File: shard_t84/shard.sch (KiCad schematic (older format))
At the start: 7 parts, among them J0 Shard, J1 ISP, U1 ATtiny84-20PU

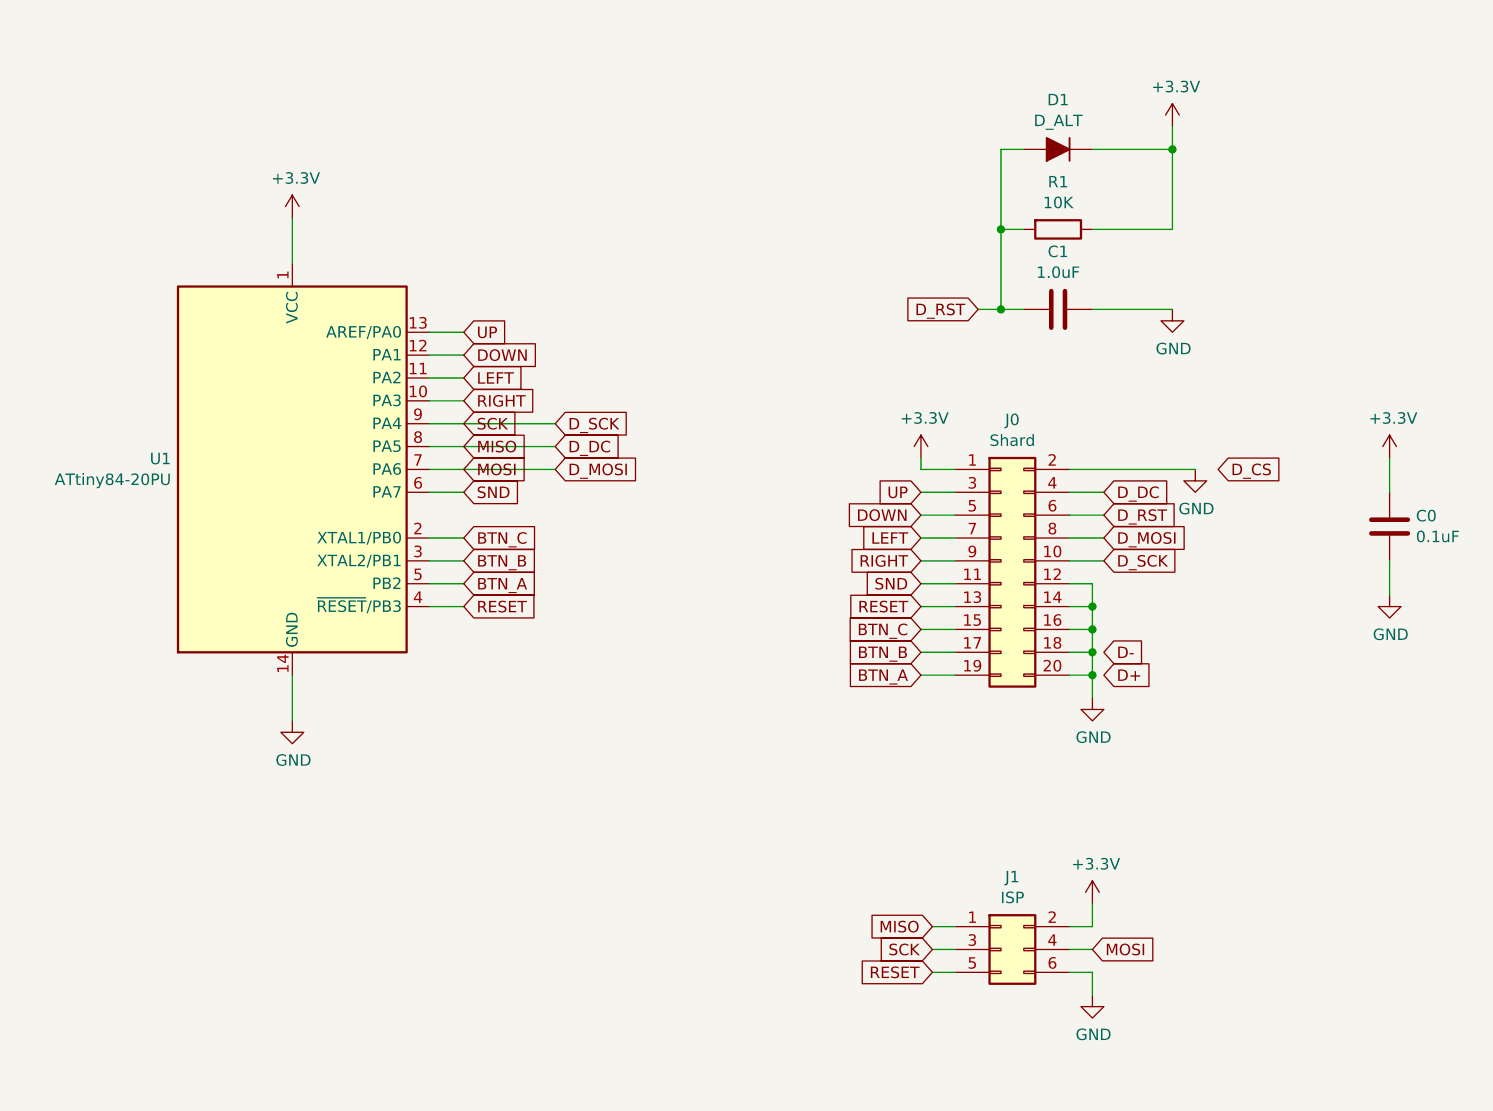
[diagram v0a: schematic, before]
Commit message: t84 shard updated for new layout
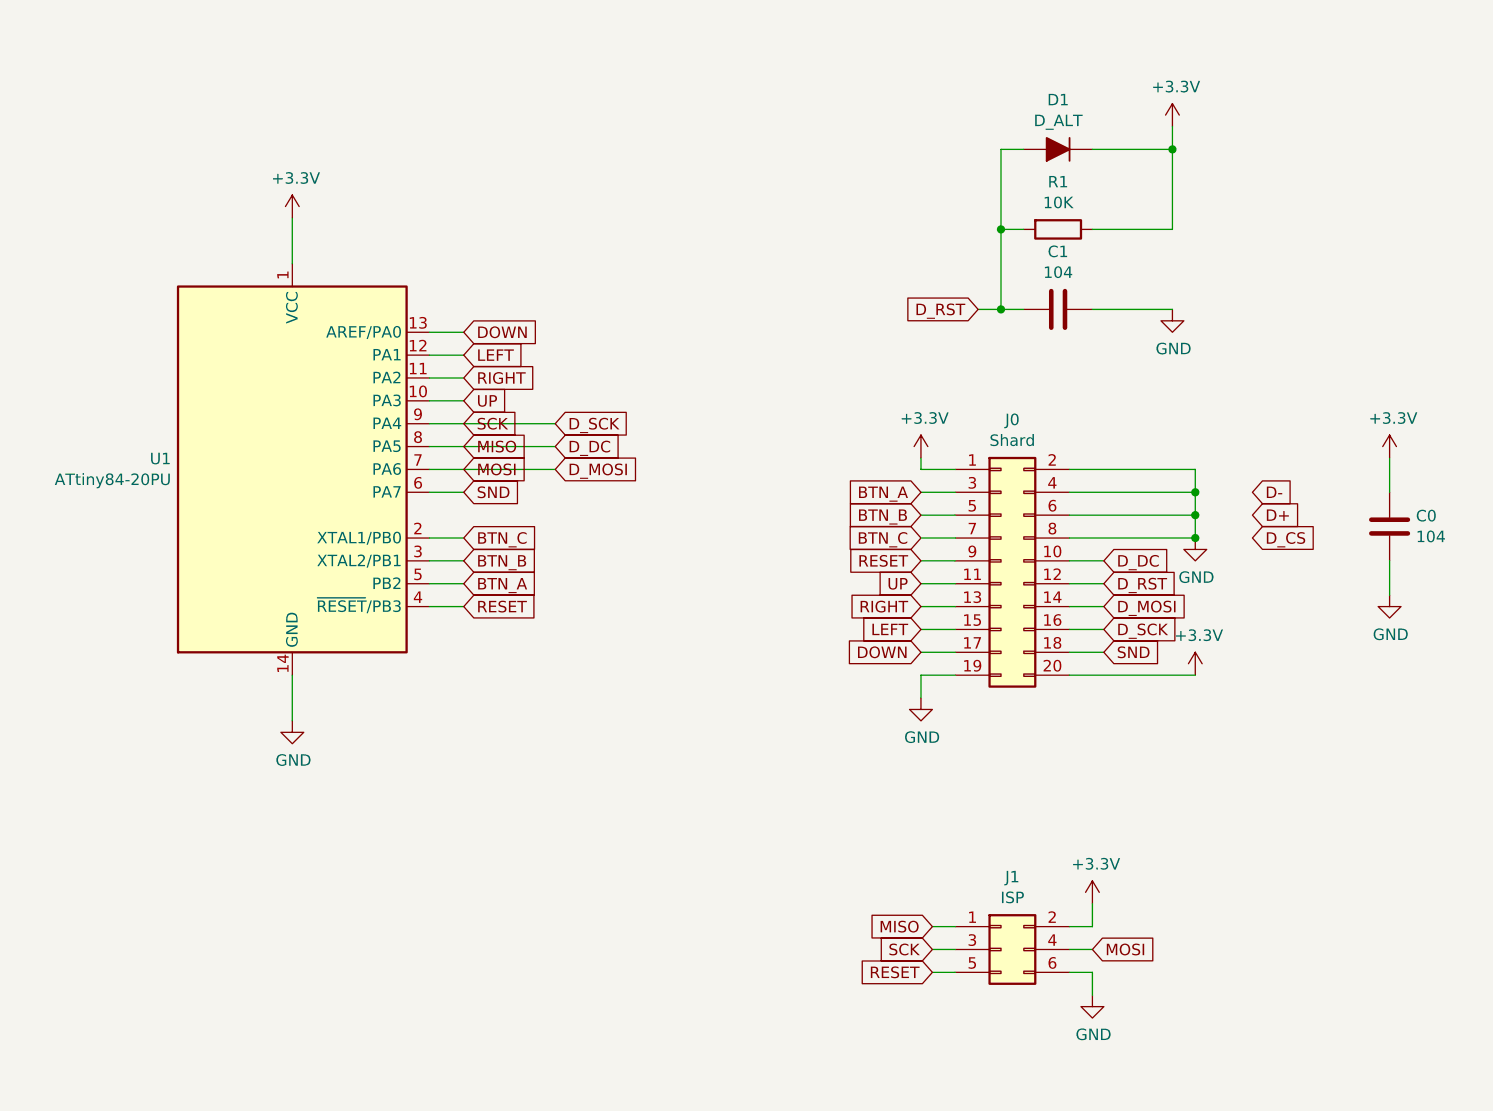
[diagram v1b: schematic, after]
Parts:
- C0: value 0.1uF -> 104
- C1: value 1.0uF -> 104
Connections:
- net +3V3: now also J0.20 (Pin_20)
- net BTN_A: now also J0.3 (Pin_3); no longer J0.19 (Pin_19)
- net BTN_B: now also J0.5 (Pin_5); no longer J0.17 (Pin_17)
- net BTN_C: now also J0.7 (Pin_7); no longer J0.15 (Pin_15)
- net DOWN: now also J0.17 (Pin_17), U1.13 (AREF/PA0); no longer J0.5 (Pin_5), U1.12 (PA1)
- net D_DC: now also J0.10 (Pin_10); no longer J0.4 (Pin_4)
- net D_MOSI: now also J0.14 (Pin_14); no longer J0.8 (Pin_8)
- net D_RST: now also J0.12 (Pin_12); no longer J0.6 (Pin_6)
- net D_SCK: now also J0.16 (Pin_16); no longer J0.10 (Pin_10)
- net GND: now also J0.19 (Pin_19), J0.4 (Pin_4), J0.6 (Pin_6), J0.8 (Pin_8); no longer J0.12 (Pin_12), J0.14 (Pin_14), J0.16 (Pin_16), J0.18 (Pin_18), J0.20 (Pin_20)
- net LEFT: now also J0.15 (Pin_15), U1.12 (PA1); no longer J0.7 (Pin_7), U1.11 (PA2)
- net RESET: now also J0.9 (Pin_9); no longer J0.13 (Pin_13)
- net RIGHT: now also J0.13 (Pin_13), U1.11 (PA2); no longer J0.9 (Pin_9), U1.10 (PA3)
- net SND: now also J0.18 (Pin_18); no longer J0.11 (Pin_11)
- net UP: now also J0.11 (Pin_11), U1.10 (PA3); no longer J0.3 (Pin_3), U1.13 (AREF/PA0)
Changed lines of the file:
@@
 P 7800 3050
 F 0 "C0" H 7915 3096 50  0000 L CNN
-F 1 "0.1uF" H 7915 3005 50  0000 L CNN
+F 1 "104" H 7915 3005 50  0000 L CNN
 F 2 "Capacitor_THT:C_Rect_L7.0mm_W2.5mm_P5.00mm" H 7838 2900 50  0001 C CNN
 F 3 "~" H 7800 3050 50  0001 C CNN
@@
 $EndComp
 $Comp
-L power:GND #PWR0102
-U 1 1 5BE69B29
-P 6500 3800
-F 0 "#PWR0102" H 6500 3550 50  0001 C CNN
-F 1 "GND" H 6505 3627 50  0000 C CNN
-F 2 "" H 6500 3800 50  0001 C CNN
-F 3 "" H 6500 3800 50  0001 C CNN
-	1    6500 3800
-	1    0    0    -1
-$EndComp
-$Comp
 L power:GND #PWR0103
 U 1 1 5BE69CAB
@@
 $EndComp
 Wire Wire Line
-	6400 3700 6500 3700
-Wire Wire Line
-	6500 3700 6500 3800
-Wire Wire Line
-	6400 3600 6500 3600
-Wire Wire Line
-	6500 3600 6500 3700
-Connection ~ 6500 3700
-Wire Wire Line
-	6400 3500 6500 3500
-Wire Wire Line
-	6500 3500 6500 3600
-Connection ~ 6500 3600
-Wire Wire Line
-	6400 3400 6500 3400
-Wire Wire Line
-	6500 3400 6500 3500
-Connection ~ 6500 3500
-Wire Wire Line
-	6400 3300 6500 3300
-Wire Wire Line
-	6500 3300 6500 3400
-Connection ~ 6500 3400
-Wire Wire Line
 	5750 2750 5750 2800
 Wire Wire Line
 	5750 2800 5900 2800
-Text GLabel 7050 2800 2    50   Input ~ 0
+Text GLabel 7200 3100 2    50   Input ~ 0
 D_CS
-Text GLabel 6550 2900 2    50   Input ~ 0
+Text GLabel 6550 3200 2    50   Input ~ 0
 D_DC
-Text GLabel 6550 3000 2    50   Input ~ 0
+Text GLabel 6550 3300 2    50   Input ~ 0
 D_RST
-Text GLabel 6550 3100 2    50   Input ~ 0
+Text GLabel 6550 3400 2    50   Input ~ 0
 D_MOSI
-Text GLabel 6550 3200 2    50   Input ~ 0
+Text GLabel 6550 3500 2    50   Input ~ 0
 D_SCK
 Wire Wire Line
-	6400 2900 6550 2900
-Wire Wire Line
-	6400 3000 6550 3000
-Wire Wire Line
-	6400 3100 6550 3100
-Wire Wire Line
 	6400 3200 6550 3200
+Text GLabel 5750 3300 0    50   Input ~ 0
+UP
+Text GLabel 5750 3600 0    50   Input ~ 0
+DOWN
+Text GLabel 5750 3500 0    50   Input ~ 0
+LEFT
+Text GLabel 5750 3400 0    50   Input ~ 0
+RIGHT
+Text GLabel 6550 3600 2    50   Input ~ 0
+SND
+Text GLabel 5750 3200 0    50   Input ~ 0
+RESET
+Text GLabel 5750 3100 0    50   Input ~ 0
+BTN_C
+Text GLabel 5750 3000 0    50   Input ~ 0
+BTN_B
 Text GLabel 5750 2900 0    50   Input ~ 0
-UP
-Text GLabel 5750 3000 0    50   Input ~ 0
-DOWN
-Text GLabel 5750 3100 0    50   Input ~ 0
-LEFT
-Text GLabel 5750 3200 0    50   Input ~ 0
-RIGHT
-Text GLabel 5750 3300 0    50   Input ~ 0
-SND
-Text GLabel 5750 3400 0    50   Input ~ 0
-RESET
-Text GLabel 5750 3500 0    50   Input ~ 0
-BTN_C
-Text GLabel 5750 3600 0    50   Input ~ 0
-BTN_B
-Text GLabel 5750 3700 0    50   Input ~ 0
 BTN_A
 Wire Wire Line
@@
 Wire Wire Line
 	7800 3200 7800 3350
-Text GLabel 6550 3700 2    50   Input ~ 0
+Text GLabel 7200 3000 2    50   Input ~ 0
 D+
-Text GLabel 6550 3600 2    50   Input ~ 0
+Text GLabel 7200 2900 2    50   Input ~ 0
 D-
 $Comp
@@
 	1    0    0    -1
 $EndComp
+Text GLabel 3750 2500 2    50   Input ~ 0
+UP
 Text GLabel 3750 2200 2    50   Input ~ 0
-UP
+DOWN
 Text GLabel 3750 2300 2    50   Input ~ 0
-DOWN
+LEFT
 Text GLabel 3750 2400 2    50   Input ~ 0
-LEFT
-Text GLabel 3750 2500 2    50   Input ~ 0
 RIGHT
 Text GLabel 3750 3100 2    50   Input ~ 0
@@
 L power:GND #PWR01
 U 1 1 5BEE8E9F
-P 6950 2800
-F 0 "#PWR01" H 6950 2550 50  0001 C CNN
-F 1 "GND" H 6955 2627 50  0000 C CNN
-F 2 "" H 6950 2800 50  0001 C CNN
-F 3 "" H 6950 2800 50  0001 C CNN
-	1    6950 2800
+P 6950 3100
+F 0 "#PWR01" H 6950 2850 50  0001 C CNN
+F 1 "GND" H 6955 2927 50  0000 C CNN
+F 2 "" H 6950 3100 50  0001 C CNN
+F 3 "" H 6950 3100 50  0001 C CNN
+	1    6950 3100
 	1    0    0    -1
 $EndComp
@@
 P 6350 2100
 F 0 "C1" V 6098 2100 50  0000 C CNN
-F 1 "1.0uF" V 6189 2100 50  0000 C CNN
+F 1 "104" V 6189 2100 50  0000 C CNN
 F 2 "Capacitor_THT:C_Rect_L7.0mm_W2.5mm_P5.00mm" H 6388 1950 50  0001 C CNN
 F 3 "~" H 6350 2100 50  0001 C CNN
@@
 Wire Wire Line
 	6400 2800 6950 2800
+$Comp
+L power:GND #PWR0102
+U 1 1 5BE9B3E3
+P 5750 3800
+F 0 "#PWR0102" H 5750 3550 50  0001 C CNN
+F 1 "GND" H 5755 3627 50  0000 C CNN
+F 2 "" H 5750 3800 50  0001 C CNN
+F 3 "" H 5750 3800 50  0001 C CNN
+	1    5750 3800
+	1    0    0    -1
+$EndComp
+Wire Wire Line
+	5750 3700 5750 3800
+$Comp
+L power:+3.3V #PWR0109
+U 1 1 5BEA0F6B
+P 6950 3700
+F 0 "#PWR0109" H 6950 3550 50  0001 C CNN
+F 1 "+3.3V" H 6965 3873 50  0000 C CNN
+F 2 "" H 6950 3700 50  0001 C CNN
+F 3 "" H 6950 3700 50  0001 C CNN
+	1    6950 3700
+	1    0    0    -1
+$EndComp
+Wire Wire Line
+	6400 3700 6950 3700
+Wire Wire Line
+	6550 3600 6400 3600
+Wire Wire Line
+	6400 3100 6950 3100
+Wire Wire Line
+	6950 3000 6950 3100
+Wire Wire Line
+	6400 3000 6950 3000
+Connection ~ 6950 3100
+Wire Wire Line
+	6950 2900 6950 3000
+Wire Wire Line
+	6400 2900 6950 2900
+Connection ~ 6950 3000
+Wire Wire Line
+	6950 2800 6950 2900
+Connection ~ 6950 2900
+Wire Wire Line
+	6400 3300 6550 3300
+Wire Wire Line
+	6400 3400 6550 3400
+Wire Wire Line
+	6400 3500 6550 3500
 $EndSCHEMATC

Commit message: updated for edge connector
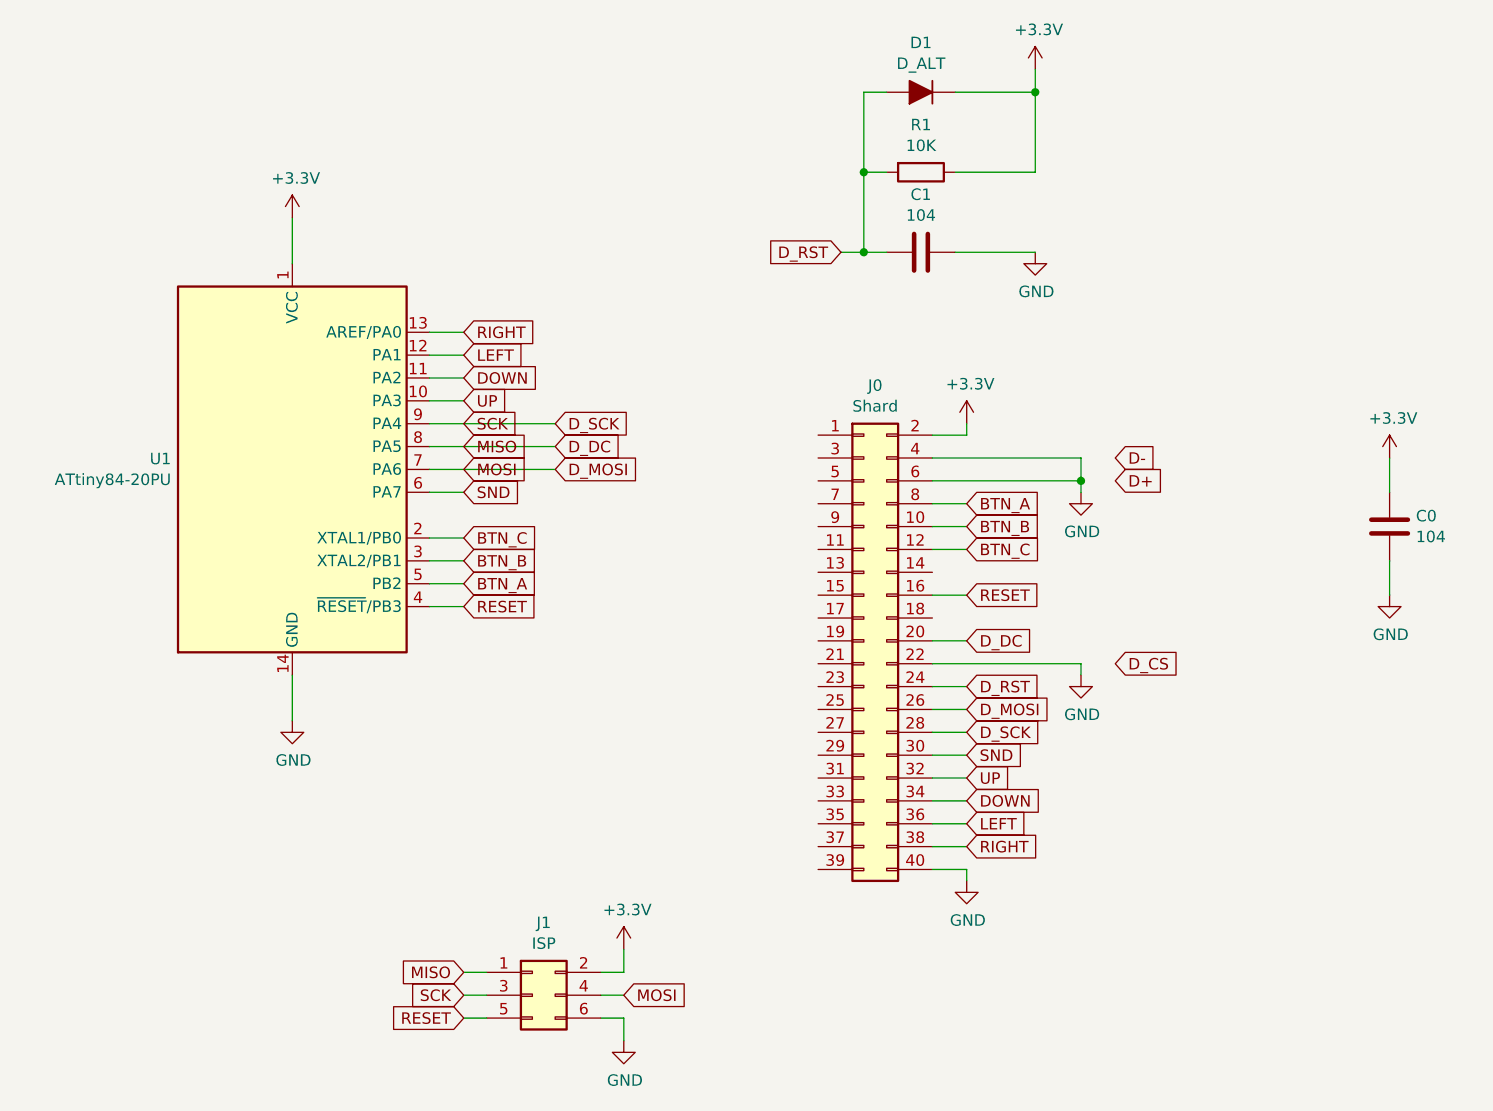
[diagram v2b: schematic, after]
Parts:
- removed J0: Shard, Connector_PinHeader_2.54mm:PinHeader_2x10_P2.54mm_Vertical, symbol Connector_Generic:Conn_02x10_Odd_Even
- added J0: Shard, Custom Footprints:Samtec_MEC8-120-02-L-D-RA1_Edge, symbol Connector_Generic:Conn_02x20_Odd_Even
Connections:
- net +3V3: now also J0.2 (Pin_2)
- net BTN_A: now also J0.8 (Pin_8)
- net BTN_B: now also J0.10 (Pin_10)
- net BTN_C: now also J0.12 (Pin_12)
- net DOWN: now also U1.11 (PA2), J0.34 (Pin_34); no longer U1.13 (AREF/PA0)
- net D_DC: now also J0.20 (Pin_20)
- net D_MOSI: now also J0.26 (Pin_26)
- net D_RST: now also J0.24 (Pin_24)
- net D_SCK: now also J0.28 (Pin_28)
- net GND: now also J0.22 (Pin_22), J0.4 (Pin_4), J0.40 (Pin_40), J0.6 (Pin_6)
- net LEFT: now also J0.36 (Pin_36)
- net RESET: now also J0.16 (Pin_16)
- net RIGHT: now also U1.13 (AREF/PA0), J0.38 (Pin_38); no longer U1.11 (PA2)
- net SND: now also J0.30 (Pin_30)
- net UP: now also J0.32 (Pin_32)
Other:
- moved on the sheet: C1, D1, J1, R1

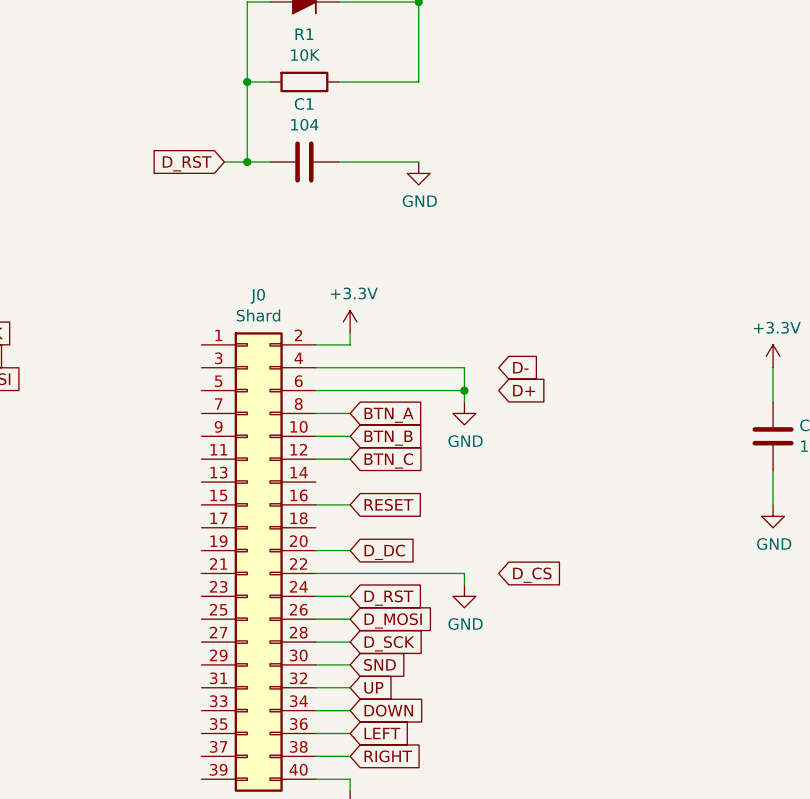
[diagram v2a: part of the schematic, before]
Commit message: fixed issues with shard
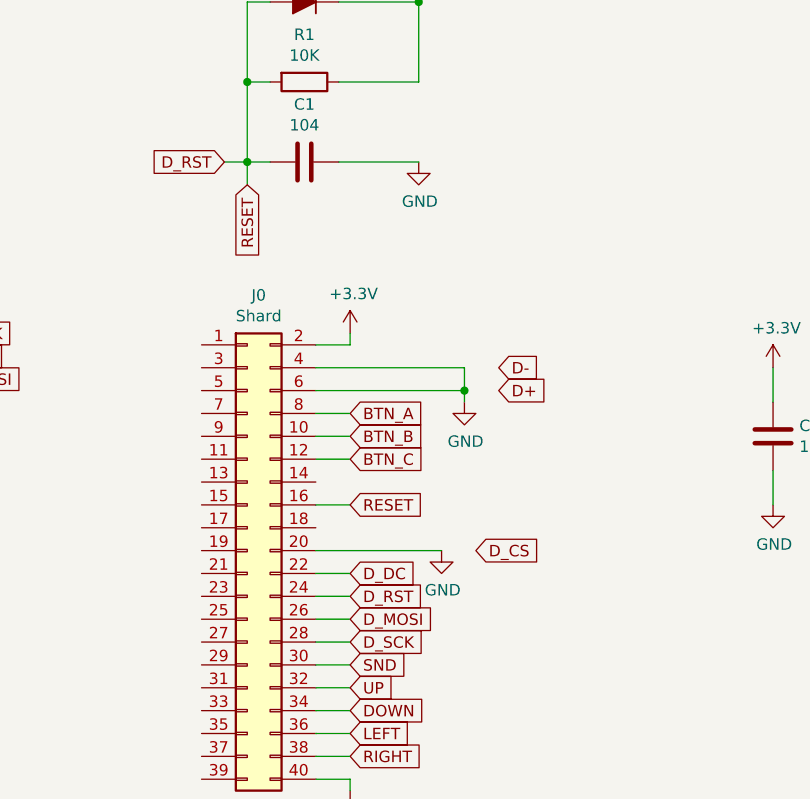
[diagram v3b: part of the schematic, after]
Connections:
- net RESET is gone; now on net D_RST: J0.16 (Pin_16), J1.5 (Pin_5), U1.4 (~RESET~/PB3)
- net D_DC: now also J0.22 (Pin_22); no longer J0.20 (Pin_20)
- net GND: now also J0.20 (Pin_20); no longer J0.22 (Pin_22)
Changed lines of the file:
@@
 	1    0    0    -1
 $EndComp
-Text GLabel 6600 3650 2    50   Input ~ 0
+Text GLabel 6500 3550 2    50   Input ~ 0
 D_CS
-Text GLabel 5950 3550 2    50   Input ~ 0
+Text GLabel 5950 3650 2    50   Input ~ 0
 D_DC
 Text GLabel 5950 3750 2    50   Input ~ 0
@@
 L power:GND #PWR0110
 U 1 1 5BF13668
-P 6450 3700
-F 0 "#PWR0110" H 6450 3450 50  0001 C CNN
-F 1 "GND" H 6455 3527 50  0000 C CNN
-F 2 "" H 6450 3700 50  0001 C CNN
-F 3 "" H 6450 3700 50  0001 C CNN
-	1    6450 3700
-	1    0    0    -1
-$EndComp
-Wire Wire Line
-	5800 3650 6450 3650
-Wire Wire Line
-	6450 3650 6450 3700
+P 6350 3550
+F 0 "#PWR0110" H 6350 3300 50  0001 C CNN
+F 1 "GND" H 6355 3377 50  0000 C CNN
+F 2 "" H 6350 3550 50  0001 C CNN
+F 3 "" H 6350 3550 50  0001 C CNN
+	1    6350 3550
+	1    0    0    -1
+$EndComp
 Wire Wire Line
 	5800 2950 5950 2950
@@
 	5800 3350 5950 3350
 Wire Wire Line
-	5800 3550 5950 3550
-Wire Wire Line
 	5800 3750 5950 3750
 Wire Wire Line
@@
 Wire Wire Line
 	5950 2650 5950 2600
+Wire Wire Line
+	5800 3650 5950 3650
+Wire Wire Line
+	5800 3550 6350 3550
+Text GLabel 5500 1950 3    50   Input ~ 0
+RESET
+Wire Wire Line
+	5500 1850 5500 1950
 $EndSCHEMATC
